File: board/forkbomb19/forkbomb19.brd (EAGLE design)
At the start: 89.2 x 57 mm, 52 parts, among them SW1 SPST_TACT-KMR2, U1 ESP-WROOM-03, X3 POT_GND, X4 POT_3V3, X5 POT_SIG

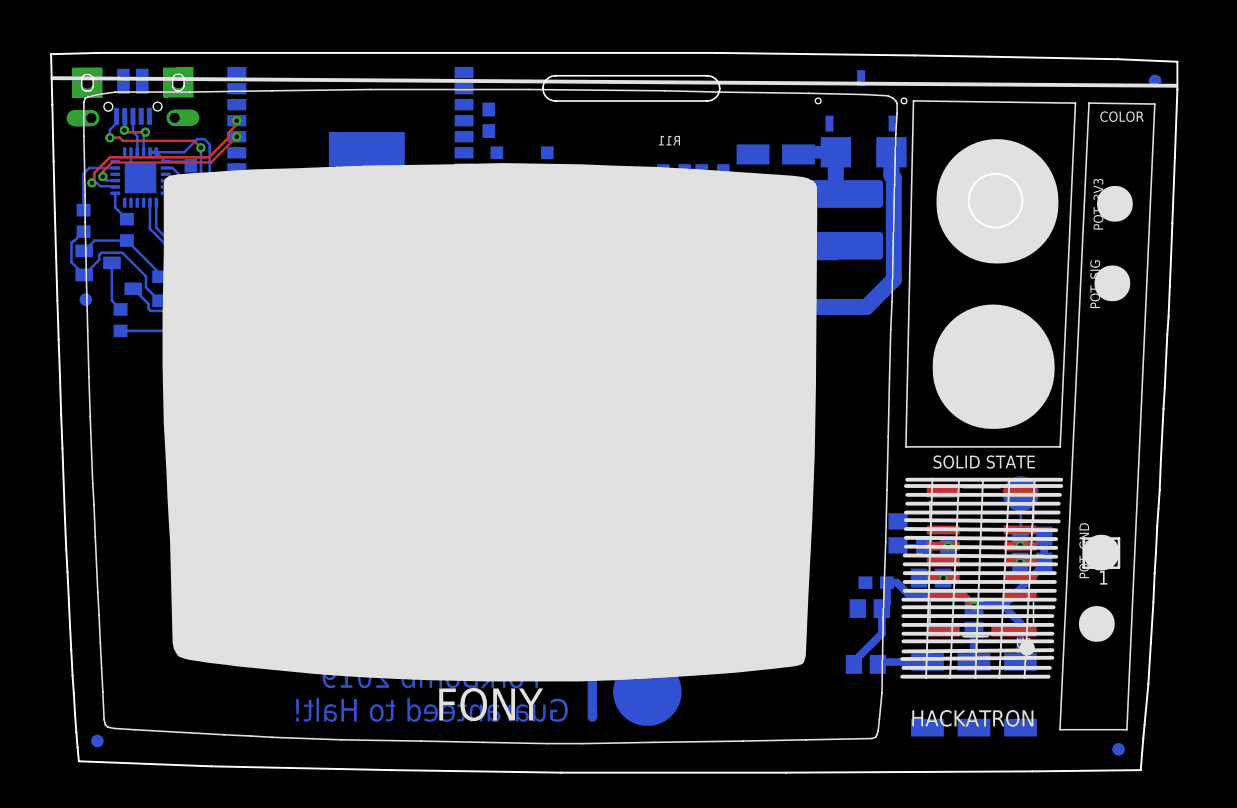
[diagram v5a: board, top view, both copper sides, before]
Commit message: created screen
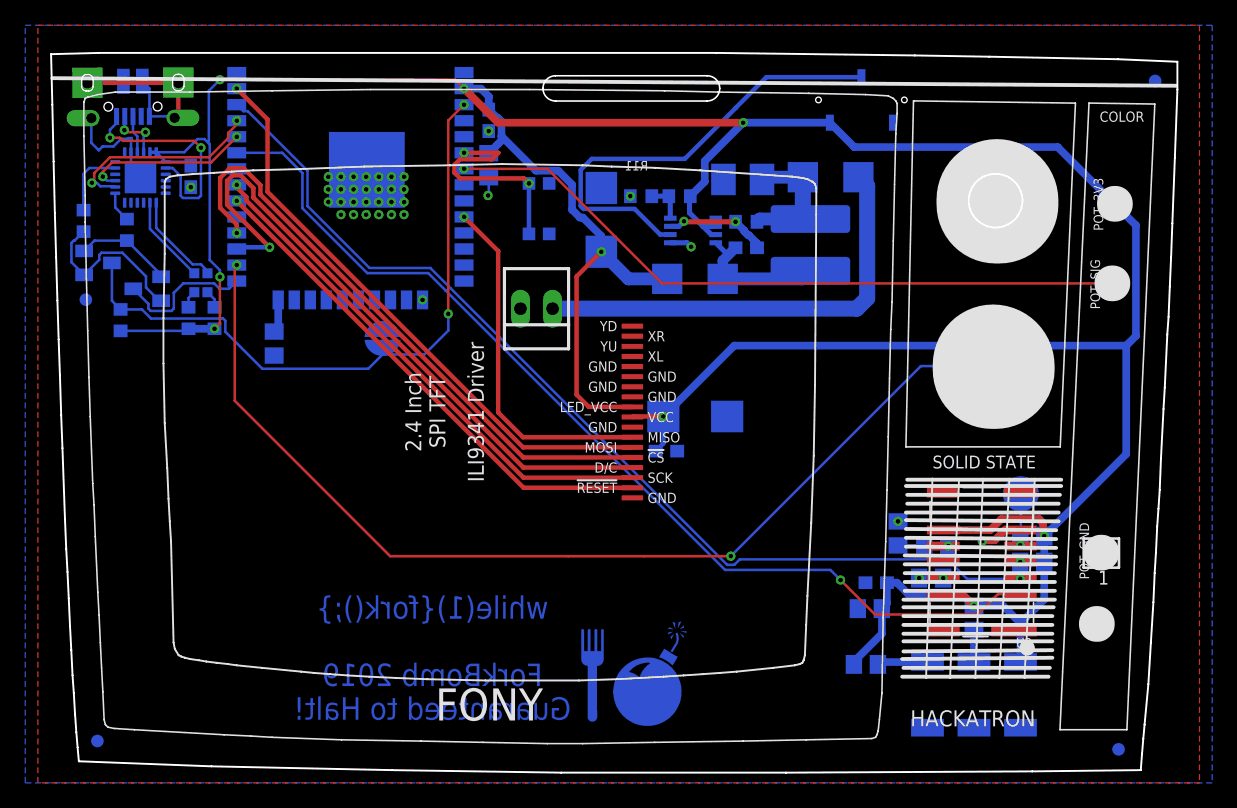
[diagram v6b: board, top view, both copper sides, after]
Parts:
- added C13: 100uF, resistor:C/6032-28R
- added C14: 100nF, resistor:C0603
- added U$2: SPI_TFT, forkbomb19:SPI_TFT
- C10: device resistor:153CLV-0405 -> resistor:T/3528-12R
- C12: value 10uF -> 100uF; device resistor:153CLV-0405 -> resistor:C/6032-28R
- moved BATT 16.0 mm to (37.5, 36.6)
- moved C12 4.11 mm to (42.6, 43.6), turned to 270 degrees
- moved SW1 3.87 mm to (37.7, 44.5), turned to 270 degrees
- moved C5 3.64 mm to (33.7, 47.9)
- moved D2 3.28 mm to (50.0, 38.9)
- moved R9 3.28 mm to (54.1, 43.4)
- moved U$1 3.28 mm to (49.9, 42.7)
- moved C11 3.28 mm to (54.1, 41.4)
- moved C10 3.28 mm to (53.8, 46.8)
- moved D1 3.28 mm to (60.8, 47.0)
- moved R10 3.28 mm to (48.8, 45.5)
- moved R11 3.28 mm to (45.8, 45.5)
- moved L1 3.28 mm to (59.2, 41.6)
- moved U$17 0.08 mm to (63.2, 53.1)
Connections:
- removed net N$16: R10.2, U$1.6, U$1.7, U$17.P$3
- net +3V3: now also C13.+, C14.1, R10.2, U$1.6, U$1.7, U$17.P$3, U$2.P$10, U$2.P$9
- net GND: now also C13.-, C14.2, U$2.P$1, U$2.P$11, U$2.P$12, U$2.P$13, U$2.P$14, U$2.P$8
- net SCRN_CLK: now also U$2.P$3
- net SCRN_CSX: now also U$2.P$5
- net SCRN_D/CX: now also U$2.P$4
- net SCRN_MISO: now also U$2.P$7
- net SCRN_MOSI: now also U$2.P$6
- net SCRN_RST: now also U$2.P$2
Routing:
- net +3V3: track 70.8 -> 286.0 mm, vias 3 -> 9
- net TOUCH1: track 0.00 -> 81.2 mm, vias 0 -> 2
- net I2C_SCL: track 0.00 -> 79.7 mm, vias 0 -> 1
- net I2C_SDA: track 0.00 -> 79.5 mm, vias 0 -> 1
- net N$4: track 0.00 -> 55.1 mm, vias 0 -> 1
- net SCRN_D/CX: track 0.00 -> 51.6 mm, vias 0 -> 1
- net EN: track 3.96 -> 52.0 mm, vias 0 -> 2
- net SCRN_CSX: track 0.00 -> 47.8 mm, vias 0 -> 1
- net SCRN_MOSI: track 0.00 -> 46.5 mm, vias 0 -> 1
- net SCRN_CLK: track 0.00 -> 41.2 mm, vias 0 -> 1
- net SCRN_RST: track 0.00 -> 40.7 mm, vias 0 -> 1
- net N$17: track 0.00 -> 36.2 mm
- net GND: track 2.93 -> 31.7 mm, vias 1 -> 36
- net SCRN_MISO: track 0.00 -> 28.0 mm, vias 0 -> 1
- net N$2: track 0.00 -> 17.5 mm, vias 0 -> 2
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- added copper zone on layer 1, net GND
- added copper zone on layer 16, net GND

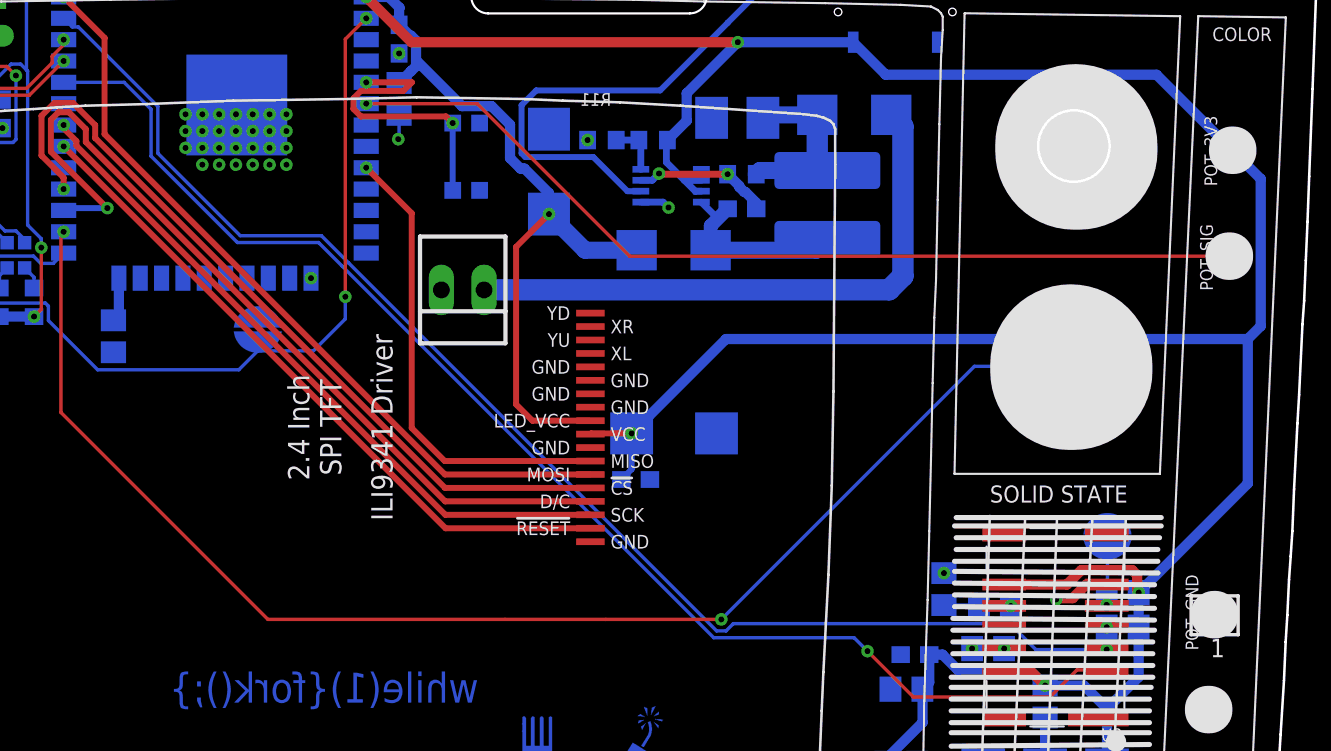
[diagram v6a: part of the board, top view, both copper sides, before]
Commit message: added touch pad
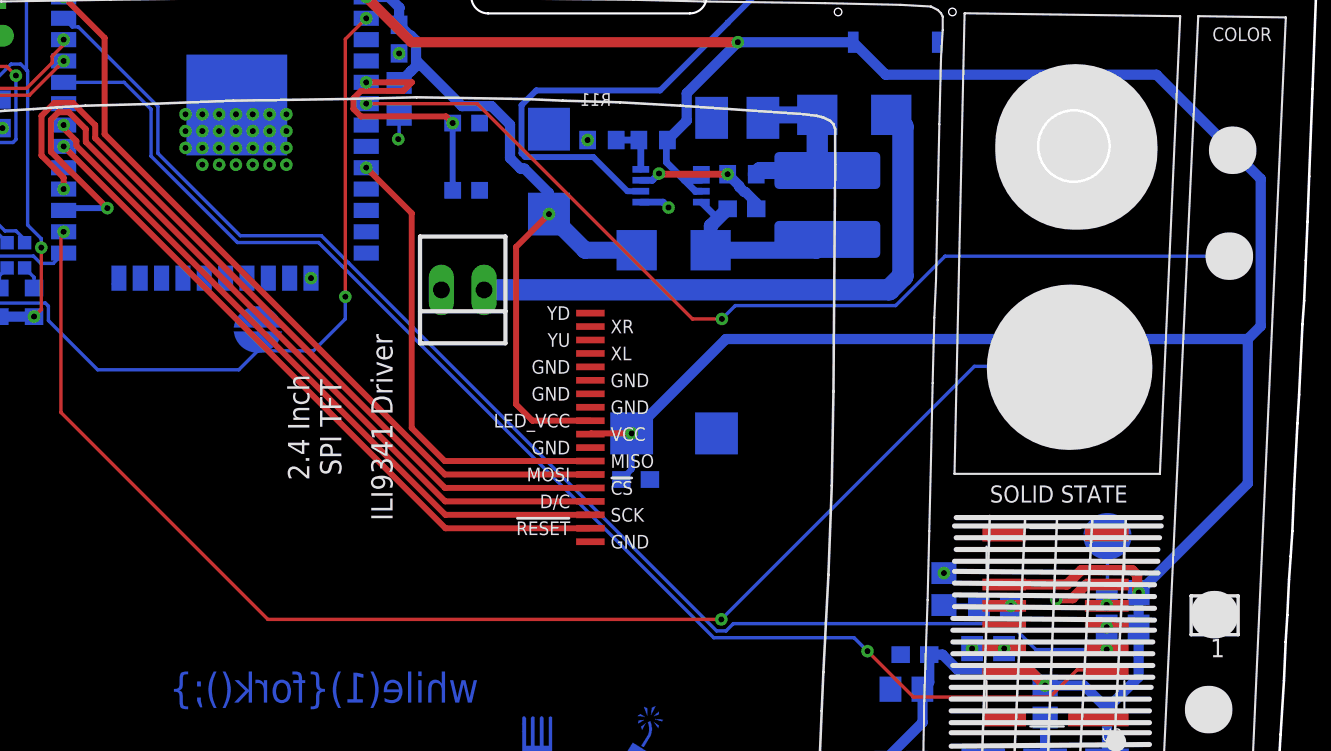
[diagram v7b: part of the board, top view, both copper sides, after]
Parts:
- removed C2: (no value), resistor:C0805
- added TOUCH: TOUCHPAD, forkbomb19:TOUCHPAD_9.5MM
- moved C3 1.07 mm to (74.6, 32.0)
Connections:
- net TOUCH1: now also TOUCH.P$1
- net TOUCH2: no longer C2.1
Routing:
- net N$4: track 55.1 -> 58.2 mm, vias 1 -> 2
- net TOUCH2: track 2.64 -> 0.45 mm
- net TOUCH1: track 81.2 -> 82.4 mm, vias 2 -> 4
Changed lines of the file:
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@@
 </polygon>
 <polygon width="0.1524" layer="21">
-<vertex x="73.6454" y="36.8092" curve="-90"/>
-<vertex x="78.4454" y="32.0092"/>
-<vertex x="78.4454" y="31.7092" curve="-90"/>
-<vertex x="73.8454" y="27.1092"/>
-<vertex x="73.5454" y="27.1092" curve="-90"/>
-<vertex x="68.9454" y="31.7092"/>
-<vertex x="68.9454" y="32.1092" curve="-90"/>
+<vertex x="73.6511" y="36.7959" curve="-90"/>
+<vertex x="78.4454" y="32.0016"/>
+<vertex x="78.4454" y="31.9124" curve="-90"/>
+<vertex x="73.6422" y="27.1092"/>
+<vertex x="73.52" y="27.1092" curve="-90"/>
+<vertex x="68.7422" y="31.887" curve="-90"/>
 </polygon>
 <wire x1="66.8454" y1="23.0092" x2="72.8454" y2="23.0092" width="0.3048" layer="21"/>
@@
 <attribute name="VALUE" x="11.2258" y="45.6336" size="0.762" layer="26" font="vector" ratio="20" rot="MR90"/>
 </element>
-<element name="C2" library="resistor" library_urn="urn:adsk.eagle:library:348" package="C0805" package3d_urn="urn:adsk.eagle:package:23617/2" value="" x="16.7142" y="33.7922" smashed="yes" rot="MR270">
-<attribute name="NAME" x="18.6954" y="32.9286" size="0.762" layer="26" font="vector" ratio="20" rot="MR270"/>
-<attribute name="VALUE" x="19.2542" y="35.0622" size="1.27" layer="28" rot="MR270"/>
-</element>
-<element name="C3" library="resistor" library_urn="urn:adsk.eagle:library:348" package="C0805" package3d_urn="urn:adsk.eagle:package:23617/2" value="" x="73.5736" y="32.005" smashed="yes" rot="MR180">
-<attribute name="NAME" x="72.3036" y="30.735" size="0.762" layer="26" font="vector" ratio="20" rot="MR180"/>
-<attribute name="VALUE" x="72.3036" y="34.545" size="1.27" layer="28" rot="MR180"/>
+<element name="C3" library="resistor" library_urn="urn:adsk.eagle:library:348" package="C0805" package3d_urn="urn:adsk.eagle:package:23617/2" value="" x="74.6404" y="32.005" smashed="yes" rot="MR180">
+<attribute name="NAME" x="73.3704" y="30.735" size="0.762" layer="26" font="vector" ratio="20" rot="MR180"/>
+<attribute name="VALUE" x="73.3704" y="34.545" size="1.27" layer="28" rot="MR180"/>
 </element>
 <element name="C4" library="resistor" library_urn="urn:adsk.eagle:library:348" package="C0603" package3d_urn="urn:adsk.eagle:package:23616/2" value="100nF" x="33.7068" y="51.4706" smashed="yes" rot="MR270">
@@
 </element>
 <element name="LOGO_R" library="forkbomb19" package="PLCC2_LED" value="" x="68.453" y="5.969" smashed="yes" rot="MR270">
-<attribute name="NAME" x="72.253" y="6.069" size="1.27" layer="22" font="vector" ratio="20" rot="MR270" align="center"/>
 <attribute name="VALUE" x="70.753" y="6.069" size="1.27" layer="22" font="vector" ratio="20" rot="MR270" align="center"/>
 </element>
 <element name="LOGO_G" library="forkbomb19" package="PLCC2_LED" value="" x="72.136" y="5.969" smashed="yes" rot="MR270">
-<attribute name="NAME" x="66.665" y="3.656" size="1.27" layer="22" font="vector" ratio="20" rot="MR270" align="center"/>
 <attribute name="VALUE" x="74.436" y="6.069" size="1.27" layer="22" font="vector" ratio="20" rot="MR270" align="center"/>
 </element>
@@
 <attribute name="OC_FARNELL" value="" x="82.2198" y="17.1958" size="1.778" layer="27" display="off"/>
 <attribute name="OC_NEWARK" value="" x="82.2198" y="17.1958" size="1.778" layer="27" display="off"/>
-<attribute name="VALUE" x="81.2546" y="15.113" size="0.762" layer="25" font="vector" ratio="20" rot="R90"/>
+<attribute name="VALUE" x="83.8962" y="14.9606" size="0.762" layer="26" font="vector" ratio="20" rot="MR90"/>
 </element>
 <element name="X4" library="con-samtec" library_urn="urn:adsk.eagle:library:184" package="TSW-101-XX-G-S" value="POT_3V3" x="83.2866" y="44.831" smashed="yes" rot="MR0">
@@
 <attribute name="OC_FARNELL" value="" x="83.2866" y="44.831" size="1.778" layer="28" rot="MR0" display="off"/>
 <attribute name="OC_NEWARK" value="" x="83.2866" y="44.831" size="1.778" layer="28" rot="MR0" display="off"/>
-<attribute name="VALUE" x="82.3722" y="42.7228" size="0.762" layer="25" font="vector" ratio="20" rot="R90"/>
+<attribute name="VALUE" x="85.0392" y="43.0022" size="0.762" layer="26" font="vector" ratio="20" rot="MR90"/>
 </element>
 <element name="X5" library="con-samtec" library_urn="urn:adsk.eagle:library:184" package="TSW-101-XX-G-S" value="POT_SIG" x="83.058" y="38.5572" smashed="yes" rot="MR0">
@@
 <attribute name="OC_FARNELL" value="" x="83.058" y="38.5572" size="1.778" layer="28" rot="MR0" display="off"/>
 <attribute name="OC_NEWARK" value="" x="83.058" y="38.5572" size="1.778" layer="28" rot="MR0" display="off"/>
-<attribute name="VALUE" x="81.3562" y="40.4622" size="0.762" layer="25" font="vector" ratio="20" rot="R270"/>
+<attribute name="VALUE" x="85.5218" y="40.5892" size="0.762" layer="26" font="vector" ratio="20" rot="MR270"/>
 </element>
 <element name="SW1" library="adafruit" library_urn="urn:adsk.eagle:library:420" package="KMR2" package3d_urn="urn:adsk.eagle:package:6240885/1" value="SPST_TACT-KMR2" x="37.6936" y="44.4754" smashed="yes" rot="MR270"/>
@@
 </element>
 <element name="U$2" library="forkbomb19" package="SPI_TFT" value="SPI_TFT" x="45.085" y="28.3718" smashed="yes" rot="R90"/>
+<element name="TOUCH" library="forkbomb19" package="TOUCHPAD_9.5MM" value="TOUCHPAD" x="73.6346" y="31.9278" smashed="yes"/>
 </elements>
 <signals>
@@
 <contactref element="U1" pad="7"/>
 <contactref element="X5" pad="1"/>
-<wire x1="83.058" y1="38.5572" x2="47.4218" y2="38.5572" width="0.2032" layer="1"/>
 <wire x1="38.3492" y1="47.6298" x2="31.7504" y2="47.6298" width="0.2032" layer="1"/>
 <via x="31.7504" y="47.6298" extent="1-16" drill="0.35"/>
-<wire x1="47.4218" y1="38.5572" x2="38.3492" y2="47.6298" width="0.2032" layer="1"/>
+<via x="52.9082" y="34.8234" extent="1-16" drill="0.35"/>
+<wire x1="53.7036" y1="35.6188" x2="52.9082" y2="34.8234" width="0.2032" layer="16"/>
+<wire x1="63.24539375" y1="35.6188" x2="53.7036" y2="35.6188" width="0.2032" layer="16"/>
+<wire x1="83.058" y1="38.5572" x2="66.18379375" y2="38.5572" width="0.2032" layer="16"/>
+<wire x1="66.18379375" y1="38.5572" x2="63.24539375" y2="35.6188" width="0.2032" layer="16"/>
+<wire x1="52.9082" y1="34.8234" x2="51.1556" y2="34.8234" width="0.2032" layer="1"/>
+<wire x1="51.1556" y1="34.8234" x2="38.3492" y2="47.6298" width="0.2032" layer="1"/>
 </signal>
 <signal name="I2C_SDA">
@@
 <contactref element="U1" pad="26"/>
 <contactref element="C3" pad="1"/>
-<wire x1="72.6236" y1="32.005" x2="67.9272625" y2="32.005" width="0.2032" layer="16"/>
+<wire x1="73.6904" y1="32.005" x2="67.9272625" y2="32.005" width="0.2032" layer="16"/>
 <wire x1="67.9272625" y1="32.005" x2="52.8736625" y2="16.9514" width="0.2032" layer="16"/>
 <via x="52.8736625" y="16.9514" extent="1-16" drill="0.35"/>
-<wire x1="52.8736625" y1="16.9514" x2="45.9994" y2="16.9514" width="0.2032" layer="1"/>
-<wire x1="45.9994" y1="16.9514" x2="40.005" y2="16.9514" width="0.2032" layer="1"/>
-<wire x1="40.005" y1="16.9514" x2="25.8984" y2="16.9514" width="0.2032" layer="1"/>
+<wire x1="52.8736625" y1="16.9514" x2="25.8984" y2="16.9514" width="0.2032" layer="1"/>
 <wire x1="25.8984" y1="16.9514" x2="13.589" y2="29.2608" width="0.2032" layer="1"/>
 <wire x1="13.589" y1="29.2608" x2="13.589" y2="39.8484" width="0.2032" layer="1"/>
 <wire x1="13.589" y1="39.8484" x2="13.7504" y2="40.0098" width="0.2032" layer="1"/>
 <via x="13.7504" y="40.0098" extent="1-16" drill="0.35"/>
+<contactref element="TOUCH" pad="P$1"/>
+<via x="73.6346" y="31.9278" extent="1-16" drill="0.35"/>
+<wire x1="73.6346" y1="31.9278" x2="73.6346" y2="31.9492" width="0.2032" layer="16"/>
+<wire x1="73.6346" y1="31.9492" x2="73.6904" y2="32.005" width="0.2032" layer="16"/>
+<via x="73.6904" y="32.005" extent="1-16" drill="0.35"/>
 </signal>
 <signal name="N$7">
@@
 <signal name="TOUCH2">
 <contactref element="U1" pad="24"/>
-<contactref element="C2" pad="1"/>
-<wire x1="17.0354" y1="37.2498" x2="17.0354" y2="35.0634" width="0.6096" layer="16"/>
-<wire x1="17.0354" y1="35.0634" x2="16.7142" y2="34.7422" width="0.6096" layer="16"/>
+<wire x1="16.7142" y1="36.9286" x2="17.0354" y2="37.2498" width="0.2032" layer="16"/>
 </signal>
 <signal name="RDY_2_SND">

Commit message: small board modifications
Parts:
- R1: value (none) -> 1k
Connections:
- net EN: now also U3.9
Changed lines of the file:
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@@
 <?xml version="1.0" encoding="utf-8"?>
 <!DOCTYPE eagle SYSTEM "eagle.dtd">
-<eagle version="9.2.2">
+<eagle version="9.3.0">
 <drawing>
 <settings>
@@
 <attribute name="VALUE" x="27.2679" y="34.1986" size="0.6096" layer="28" font="vector" ratio="20" rot="MR270" align="top-center"/>
 </element>
-<element name="R1" library="resistor" library_urn="urn:adsk.eagle:library:348" package="R0603" package3d_urn="urn:adsk.eagle:package:23555/2" value="" x="4.5476" y="35.6464" smashed="yes" rot="MR270">
+<element name="R1" library="resistor" library_urn="urn:adsk.eagle:library:348" package="R0603" package3d_urn="urn:adsk.eagle:package:23555/2" value="1k" x="4.5476" y="35.6464" smashed="yes" rot="MR270">
 <attribute name="NAME" x="3.5712" y="34.0116" size="0.762" layer="26" font="vector" ratio="20" rot="MR180"/>
 <attribute name="VALUE" x="7.0876" y="36.2814" size="1.27" layer="28" rot="MR270"/>
@@
 <wire x1="30.5054" y1="34.8234" x2="30.5054" y2="36.1442" width="0.2032" layer="16"/>
 <wire x1="28.6106" y1="32.9286" x2="30.5054" y2="34.8234" width="0.2032" layer="16"/>
+<contactref element="U3" pad="9"/>
+<wire x1="3.8648" y1="40.178" x2="8.1252" y2="47.194" width="0" layer="19" extent="16-16"/>
 </signal>
 <signal name="N$2">
